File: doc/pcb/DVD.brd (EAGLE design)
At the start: 53.7 x 42.9 mm, 48 parts, among them IC1 7805, IC2 74HC14N

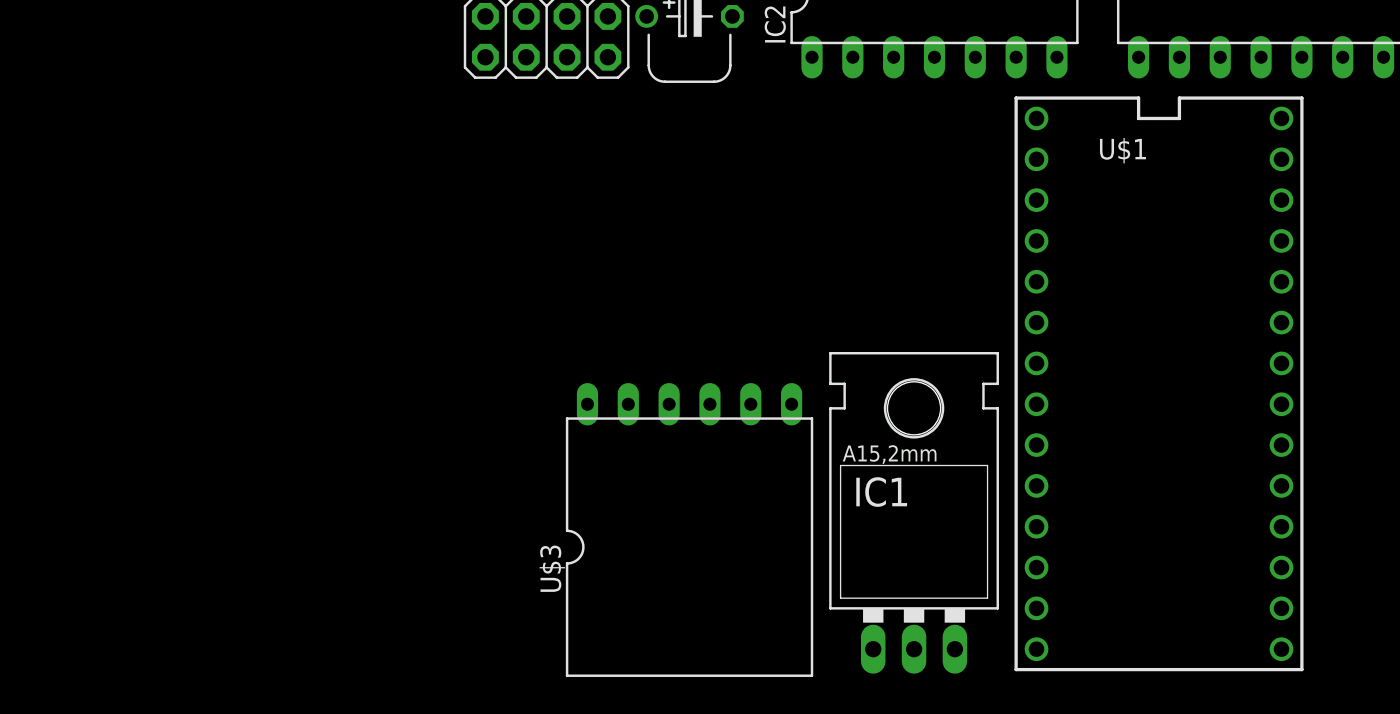
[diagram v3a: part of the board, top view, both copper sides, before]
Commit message: bigger pads for Teensy
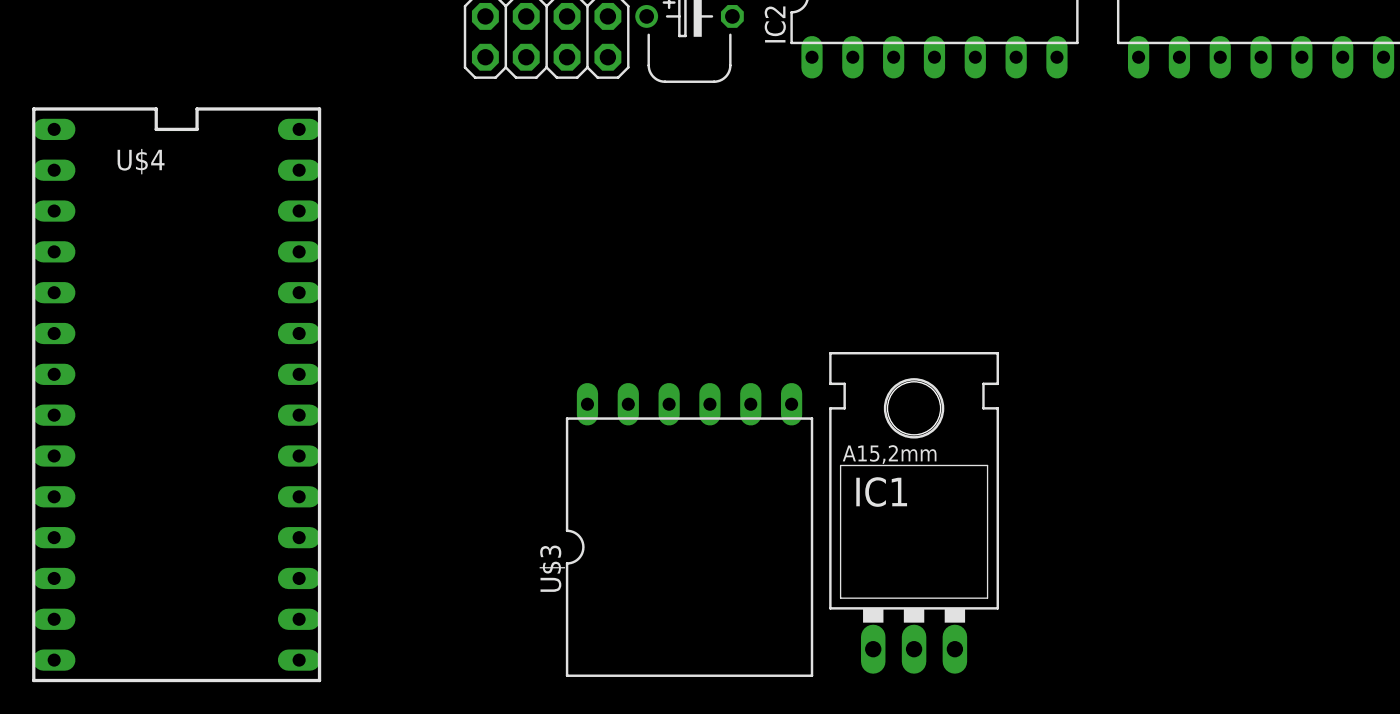
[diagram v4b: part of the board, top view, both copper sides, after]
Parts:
- removed U$1: TEENSY_3.1_BASIC_DVD, Teensy_3_Series_Board_v1.0:TEENSY_3.1_BASIC_DVD
- added U$4: TEENSY_3.1_BASIC_DVD_BP, Teensy_3_Series_Board_v1.0:TEENSY_3.1_BASIC_DVD_BIGPADS
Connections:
- net +3V3: now also U$4.3.3V; no longer U$1.3.3V
- net AGND: now also U$4.AGND; no longer U$1.AGND
- net CE: now also U$4.8; no longer U$1.8
- net CSN_RADIO: now also U$4.10; no longer U$1.10
- net CSN_SD: now also U$4.9; no longer U$1.9
- net D4_IR: now also U$4.4; no longer U$1.4
- net GND: now also U$4.GND; no longer U$1.GND
- net IN1: now also U$4.23/A9; no longer U$1.23/A9
- net IN2: now also U$4.22/A8; no longer U$1.22/A8
- net MISO: now also U$4.12; no longer U$1.12
- net MOSI: now also U$4.11; no longer U$1.11
- net N$1: now also U$4.VIN; no longer U$1.VIN
- net N$10: now also U$4.15/A1; no longer U$1.15/A1
- net N$11: now also U$4.16/A2; no longer U$1.16/A2
- net N$18: now also U$4.0; no longer U$1.0
- net N$19: now also U$4.1; no longer U$1.1
- net N$20: now also U$4.2; no longer U$1.2
- net N$21: now also U$4.6; no longer U$1.6
- net N$22: now also U$4.7; no longer U$1.7
- net N$3: now also U$4.5; no longer U$1.5
- net N$6: now also U$4.17/A3; no longer U$1.17/A3
- net N$9: now also U$4.13; no longer U$1.13
- net PWM: now also U$4.21/A7; no longer U$1.21/A7
- net SCK: now also U$4.14/A0; no longer U$1.14/A0
- net SCL: now also U$4.19/A5; no longer U$1.19/A5
- net SDA: now also U$4.18/A4; no longer U$1.18/A4
- net SPEED_SENSOR: now also U$4.3; no longer U$1.3
- net STBY: now also U$4.20/A6; no longer U$1.20/A6

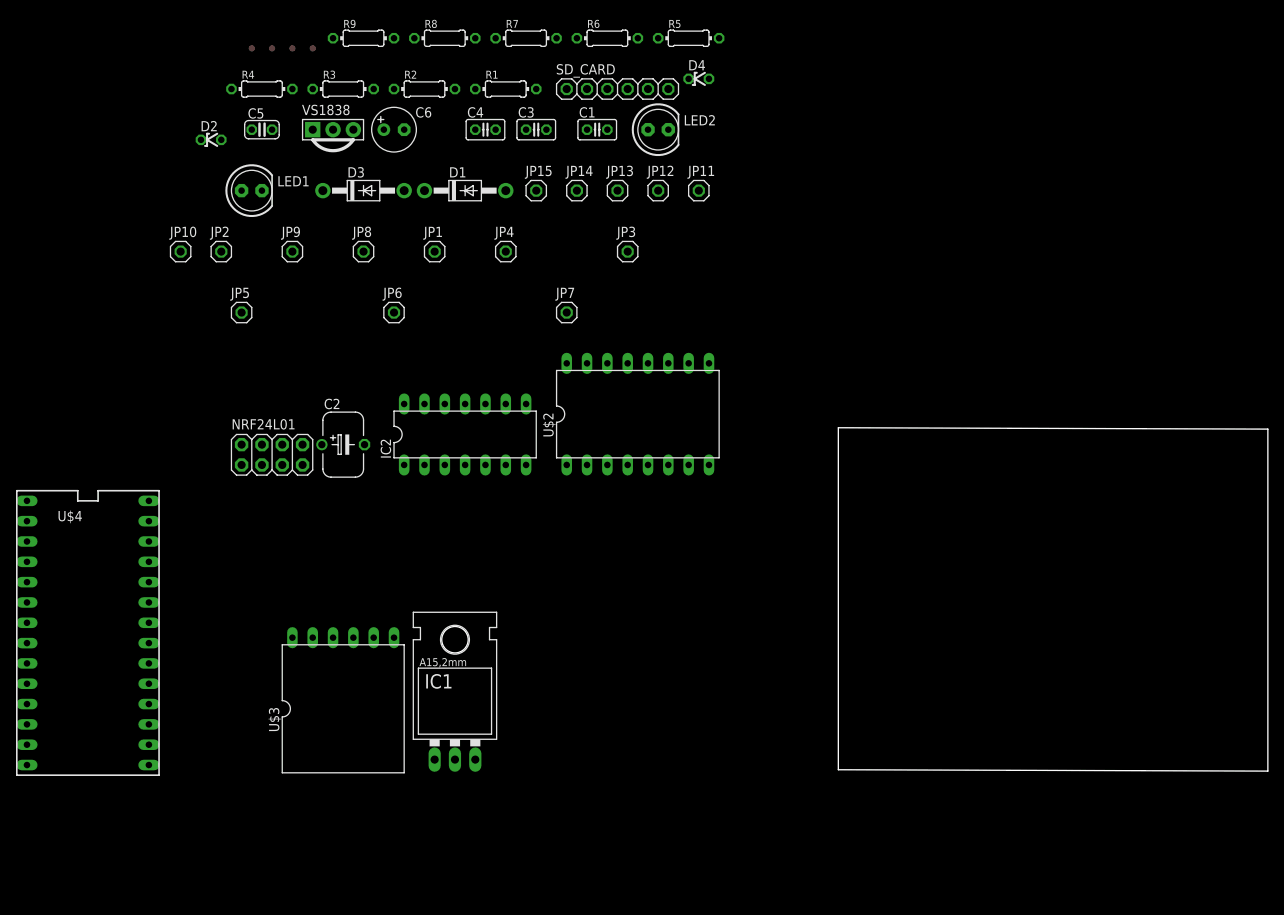
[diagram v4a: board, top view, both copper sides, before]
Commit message: Redrawn Chassis Picture, fixed schematic and created Board
Please review and give comments
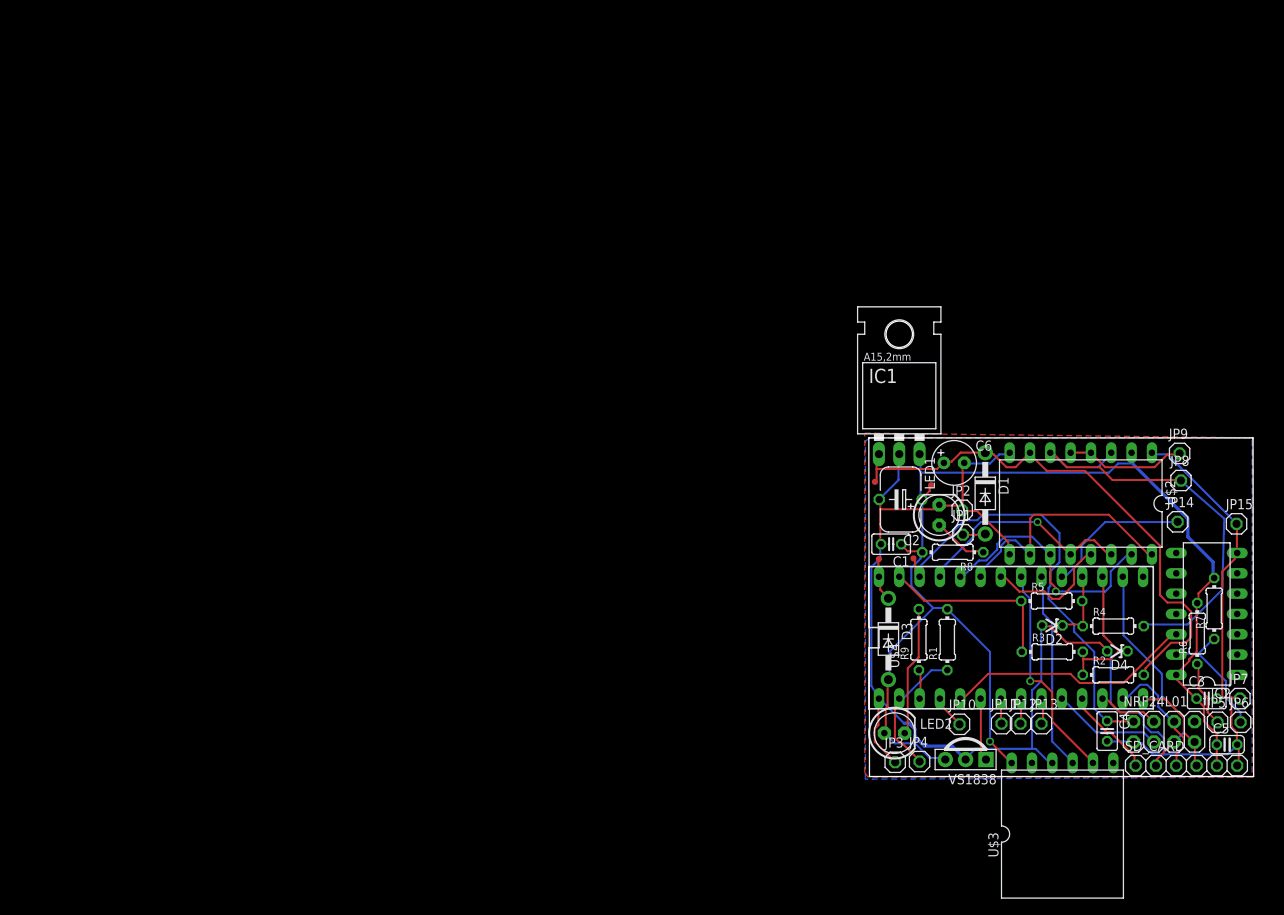
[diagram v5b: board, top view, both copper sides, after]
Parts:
- moved C5 143.0 mm to (49.5, 4.41)
- moved JP5 132.3 mm to (48.3, 7.20)
- moved R4 125.8 mm to (35.3, 19.2)
- moved D2 121.4 mm to (27.7, 19.3), turned to 180 degrees
- moved JP6 117.6 mm to (51.2, 7.20)
- moved NRF24L01 116.7 mm to (41.6, 6.01)
- moved U$4 115.4 mm to (22.5, 17.8), turned to 90 degrees
- moved JP10 113.9 mm to (16.1, 6.95)
- moved JP9 113.7 mm to (43.6, 40.8)
- moved R3 113.2 mm to (27.7, 16.0)
- moved R2 113.0 mm to (35.3, 13.1)
- moved R7 111.7 mm to (47.9, 21.4), turned to 90 degrees
- moved VS1838 111.6 mm to (16.8, 2.55), turned to 180 degrees
- moved SD_CARD 110.5 mm to (44.4, 1.79)
- moved C3 109.9 mm to (47.0, 10.2)
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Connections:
- net +5V: now also SD_CARD.5
- net GND: now also JP15.1
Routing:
- net GND: track 0.00 -> 210.5 mm
- net +5V: track 0.00 -> 152.6 mm, vias 0 -> 1
- net V+: track 0.00 -> 68.9 mm
- net +3V3: track 0.00 -> 55.7 mm
- net JP8: track 0.00 -> 55.0 mm
- net IN2: track 0.00 -> 32.1 mm, vias 0 -> 1
- net PWM: track 0.00 -> 31.5 mm
- net SPEED_SENSOR: track 0.00 -> 31.3 mm
- net IN1: track 0.00 -> 28.5 mm, vias 0 -> 1
- net SCK: track 0.00 -> 28.3 mm
- net SCL: track 0.00 -> 27.9 mm, vias 0 -> 1
- net SDA: track 0.00 -> 25.0 mm
- net AGND: track 0.00 -> 23.0 mm
- net N$10: track 0.00 -> 19.3 mm
- net N$6: track 0.00 -> 18.4 mm
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- added copper zone on layer 1, net GND
- added copper zone on layer 16, net GND
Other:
- board size 53.7 x 42.9 mm -> 48.1 x 42.3 mm

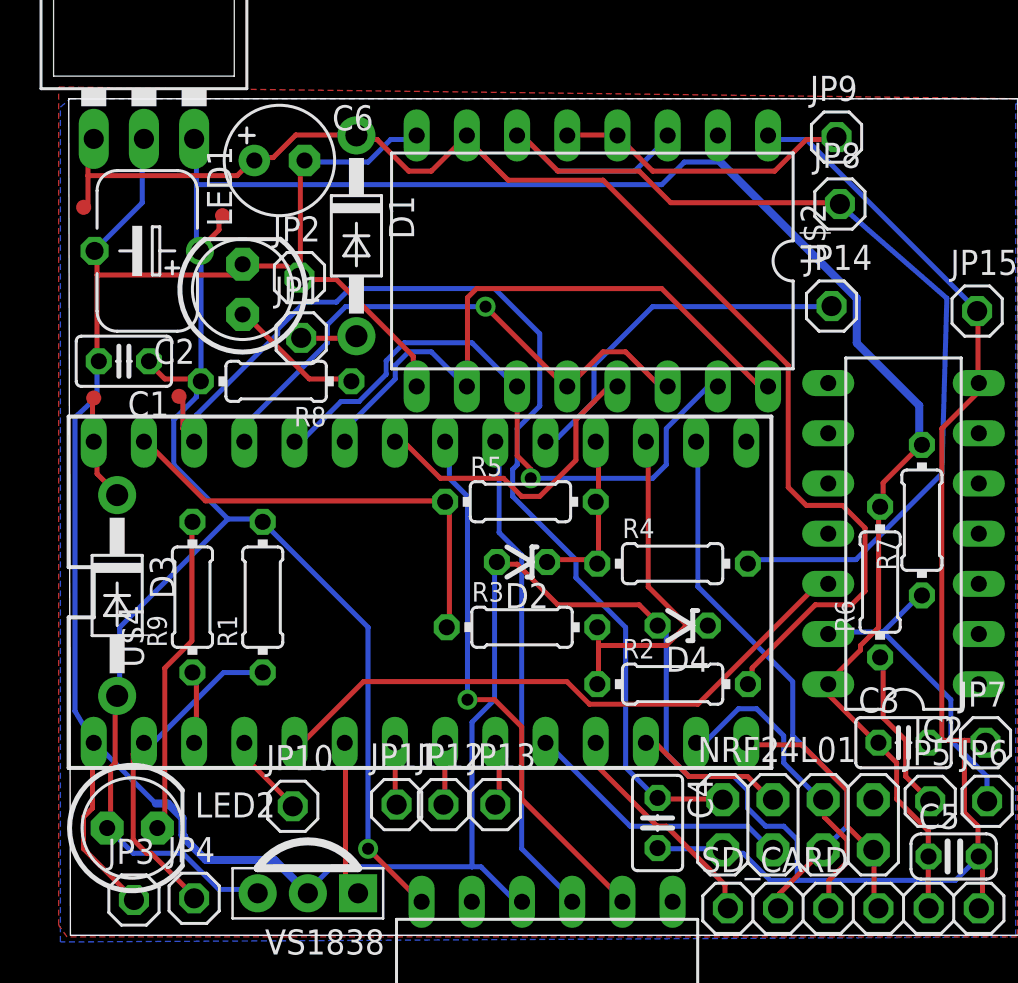
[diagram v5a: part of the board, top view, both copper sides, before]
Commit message: Schematics and PCB Updates
Schematics:
- connected all unused gates of 7414 to GND because open
  inputs may draw a lot of current
- renamed net for PickUp+ so that I can find it in the PCB
- went through ERC

PCB:
- made some tracks wider (power tracks)
- fixed DRC errors, default ones and also from the PCB
  manufacturer.
  *****NOTE****** 200+ DRC for the solder mask still
  *************** present.  I only fixed the ones for
  *************** the tracks and dimensions
- I had the copper pour up to the board outer dimension
  but that got reset when loading the DRC rules from
  dirty cheap PCBs (the manufacturer, see their "about"
  page)
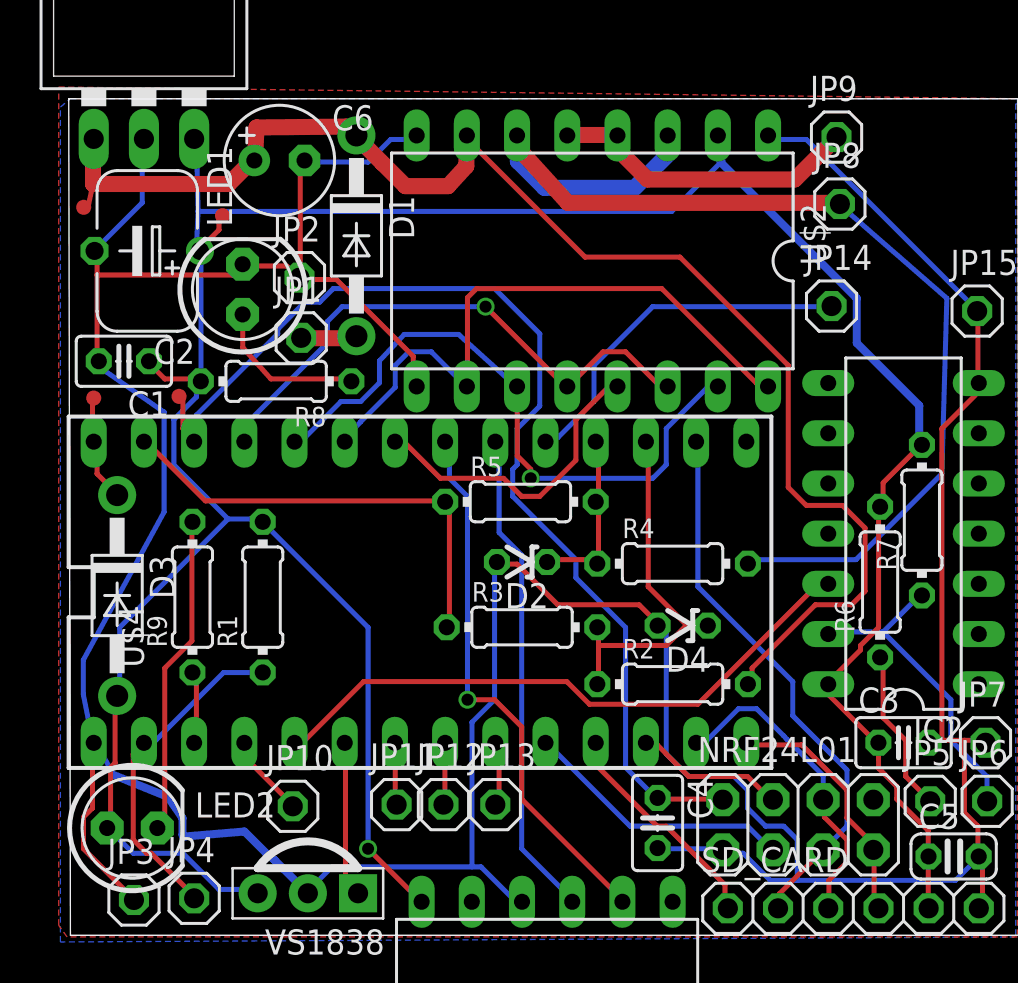
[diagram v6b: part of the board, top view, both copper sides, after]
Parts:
- LED1: value (none) -> Amber
- LED2: value (none) -> Green
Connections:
- net N$5 renamed PICKUP_PLUS
- removed net N$9: U$4.13
- net GND: now also IC2.1, IC2.11, IC2.3, IC2.5, IC2.9
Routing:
- net V+: track 68.9 -> 71.5 mm
- net GND: track 210.5 -> 212.8 mm
- net JP8: track 55.0 -> 57.1 mm
- net ENGINE1: track 15.1 -> 16.2 mm
- net N$7: track 6.91 -> 7.95 mm
- net +5V: track 152.6 -> 153.4 mm
- net IN2: track 32.1 -> 32.6 mm

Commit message: PCB updates only
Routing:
- net IN1: track 28.6 -> 30.3 mm
- net N$10: track 19.3 -> 19.8 mm
- net AGND: track 23.0 -> 23.5 mm
